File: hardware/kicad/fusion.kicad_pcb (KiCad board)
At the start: 2 copper layers, 33 x 59.9 mm, 36 parts, among them J1 BATTERY, J2 LSM6DSOX, J3 PICKIT, J4 HC-05, J5 FLEX, J7 FTDI, SW1 BUTTON, SW2 POWER, SW3 UART, U1 MCP1603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

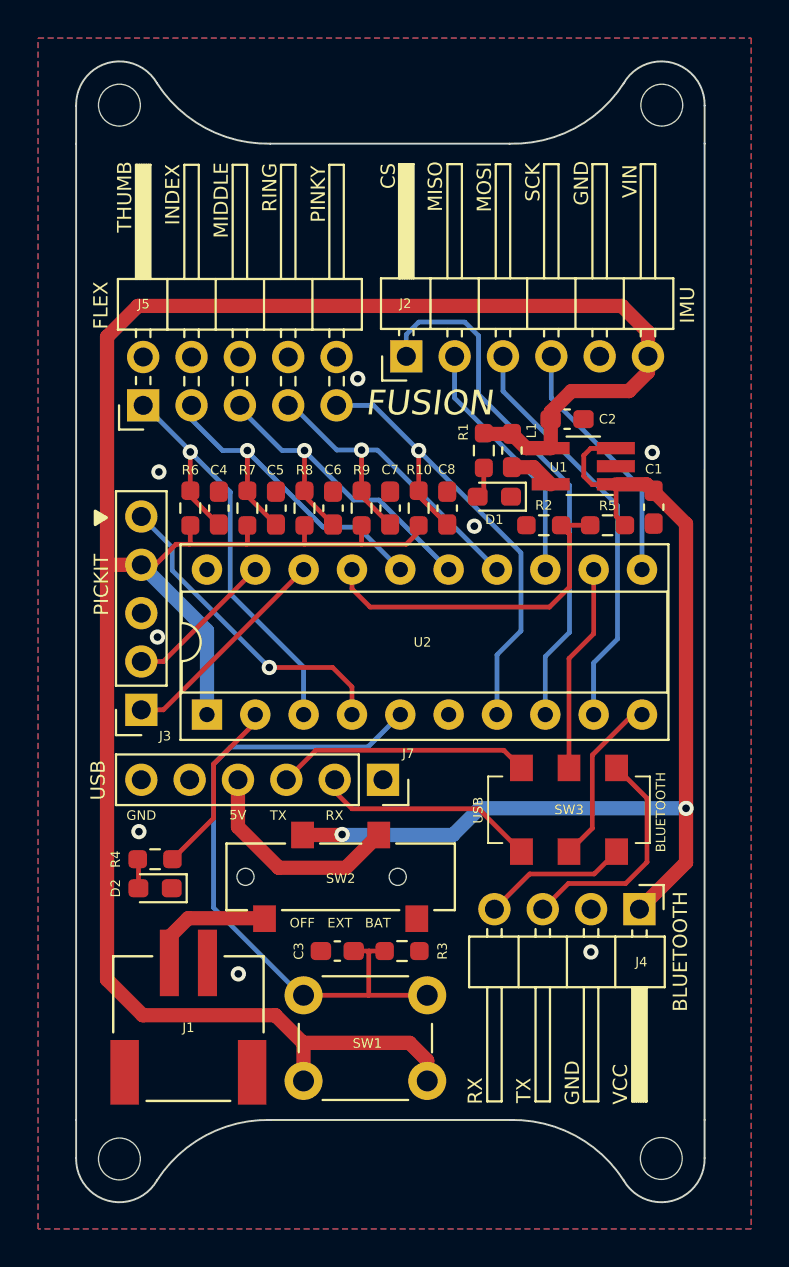
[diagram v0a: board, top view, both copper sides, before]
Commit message: Better ground stitching and silk fix for power switch
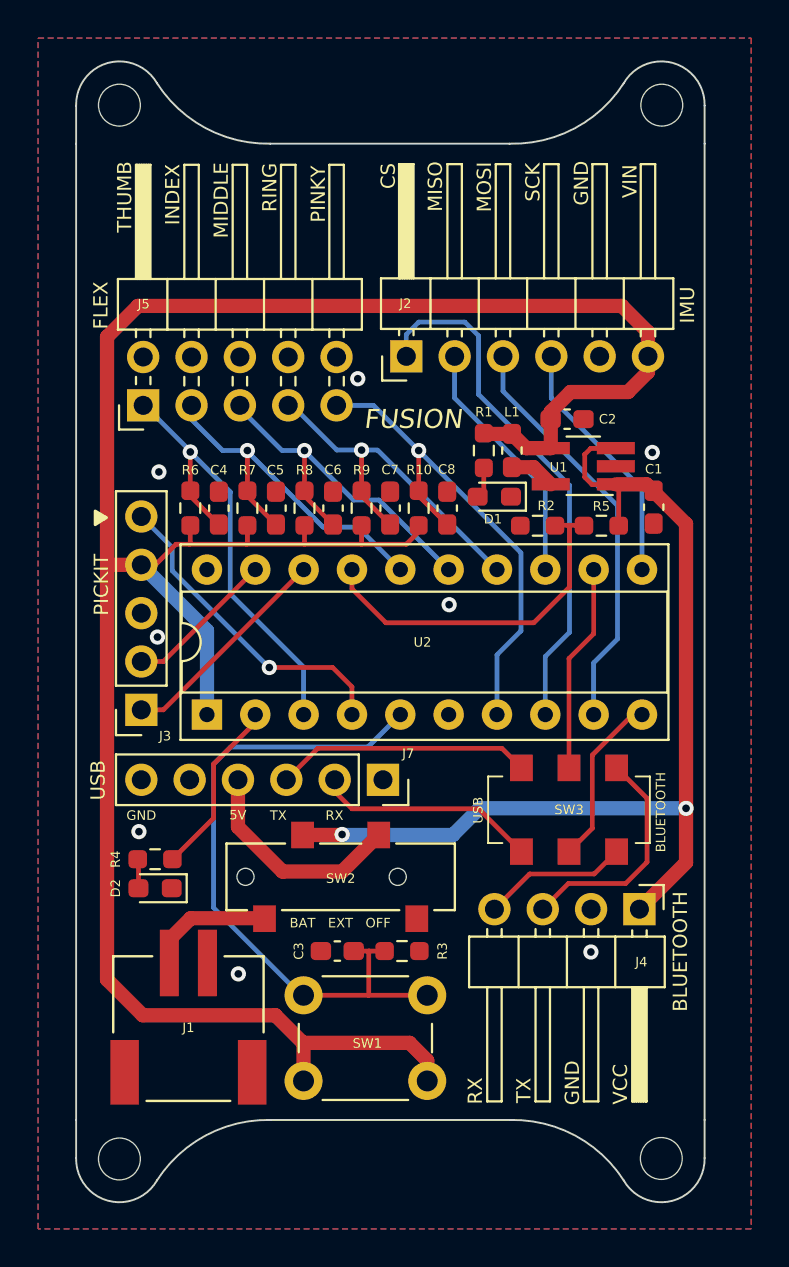
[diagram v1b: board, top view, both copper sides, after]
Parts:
- moved R5 0.33 mm to (164.6, 88.1)
- moved R2 0.33 mm to (161.2, 88.1)
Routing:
- net Net-(J1-Pad1): track 6.68 -> 5.38 mm
- net USB_RX: track 11.7 -> 11.1 mm
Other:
- board text added: "BAT EXT OFF"
- board text removed: "OFF EXT BAT"

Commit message: Change LED resistors to 200R (DigiKey availability)
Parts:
- R1, R4: value 270R -> 200R
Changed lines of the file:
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@@
       (effects (font (size 0.5 0.5) (thickness 0.1)))
     )
-    (fp_text value "270R" (at 0 1.43) (layer "F.Fab")
+    (fp_text value "200R" (at 0 1.43) (layer "F.Fab")
       (effects (font (size 1 1) (thickness 0.15)))
     )
@@
       (effects (font (size 0.5 0.5) (thickness 0.1)))
     )
-    (fp_text value "270R" (at 0 1.43 90) (layer "F.Fab")
-      (effects (font (size 1 1) (thickness 0.15)))
-    )
+    (fp_text value "200R" (at 0 1.43 90) (layer "F.Fab")
+      (effects (font (size 1 1) (thickness 0.15)))
+    )

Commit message: Implement Chung's feedback for PCB
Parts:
- moved R1 21.9 mm to (163.1, 105.5), turned to 0 degrees
- moved C2 21.0 mm to (167.1, 103.1), turned to 90 degrees
- moved L1 19.8 mm to (165.6, 103.0), turned to -90 degrees
- moved D1 19.0 mm to (159.7, 105.5), turned to 0 degrees
- moved C1 18.4 mm to (158.1, 103.0)
- moved U1 18.1 mm to (161.8, 103.0), turned to 0 degrees
- moved SW3 17.6 mm to (163.1, 85.4)
- moved R5 13.4 mm to (159.7, 100.5), turned to 0 degrees
- moved R2 12.6 mm to (163.1, 100.5), turned to 0 degrees
- moved REF** 1.00 mm to (139.3, 67.0)
- moved REF** 1.00 mm to (167.8, 67.0)
- moved J2 0.78 mm to (154.2, 80.0)
- moved J5 0.78 mm to (140.4, 82.5)
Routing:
- net BT_RX: track 7.67 -> 26.7 mm, vias 0 -> 1
- net BT_TX: track 12.1 -> 31.0 mm, vias 0 -> 1
- net VDC: track 53.3 -> 37.1 mm
- net USB_TX: track 13.5 -> 24.5 mm
- net USB_RX: track 11.1 -> 18.8 mm
- net RX: track 11.0 -> 7.55 mm
- net +3V3: track 129.3 -> 125.9 mm
- net TX: track 8.59 -> 11.8 mm
- net GNDREF: track 0.00 -> 2.35 mm, vias 8 -> 12
- net MCLR: track 17.0 -> 18.4 mm
- net CS: track 27.9 -> 26.7 mm
- net PINKY: track 26.2 -> 27.2 mm
- net SCK: track 13.2 -> 12.4 mm
- net MISO: track 13.2 -> 12.4 mm
- net MOSI: track 21.8 -> 21.1 mm
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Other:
- board size 33 x 59.9 mm -> 33 x 58.9 mm
- board text added: "v1.0"

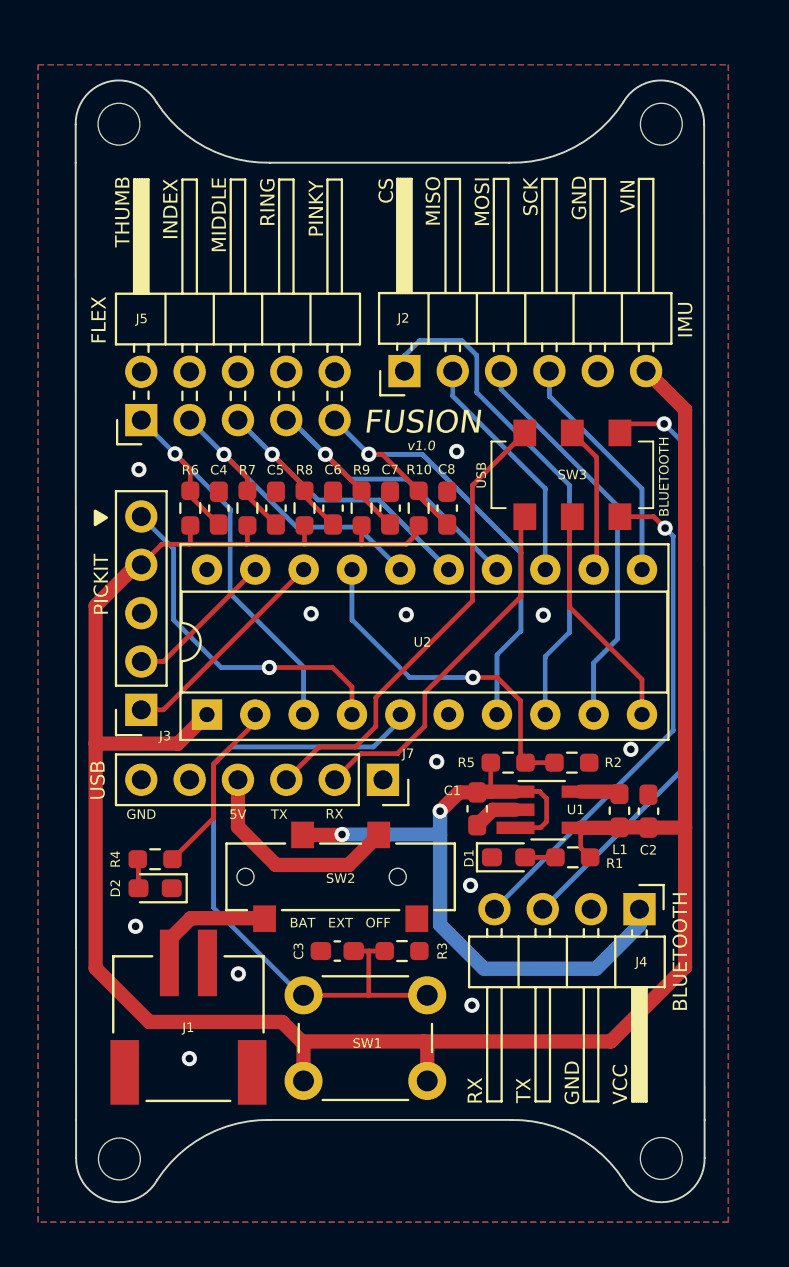
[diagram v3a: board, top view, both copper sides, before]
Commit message: small routing changes
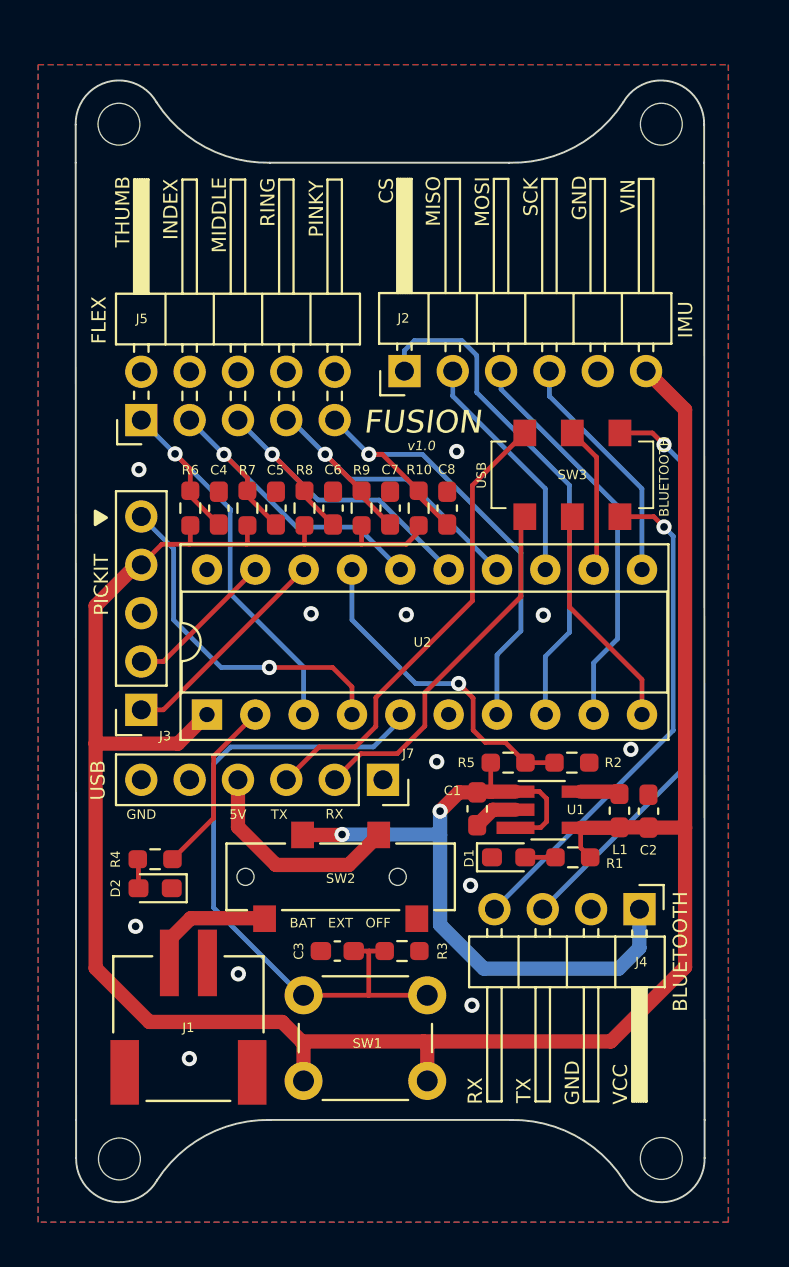
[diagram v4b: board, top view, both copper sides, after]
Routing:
- net VBAT_ADC: track 18.1 -> 17.4 mm
- net VDC: track 37.1 -> 37.7 mm
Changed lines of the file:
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@@
     (effects (font (size 0.5 0.5) (thickness 0.1)))
   )
+  (segment (start 154.25 78.8712) (end 154.25 79.95) (width 0.25) (layer "B.Cu") (net 1))
+  (segment (start 157.275 78.35) (end 154.7712 78.35) (width 0.25) (layer "B.Cu") (net 1))
+  (segment (start 154.7712 78.35) (end 154.25 78.8712) (width 0.25) (layer "B.Cu") (net 1))
+  (segment (start 161.655 98) (end 161.655 94.945) (width 0.25) (layer "B.Cu") (net 1))
+  (segment (start 158.05 79.125) (end 157.275 78.35) (width 0.25) (layer "B.Cu") (net 1))
+  (segment (start 162.925 85.95) (end 158.05 81.075) (width 0.25) (layer "B.Cu") (net 1))
   (segment (start 162.925 93.675) (end 162.925 85.95) (width 0.25) (layer "B.Cu") (net 1))
-  (segment (start 158.05 79.125) (end 157.275 78.35) (width 0.25) (layer "B.Cu") (net 1))
-  (segment (start 155.05 78.35) (end 154.25 79.15) (width 0.25) (layer "B.Cu") (net 1))
+  (segment (start 161.655 94.945) (end 162.925 93.675) (width 0.25) (layer "B.Cu") (net 1))
   (segment (start 158.05 81.075) (end 158.05 79.125) (width 0.25) (layer "B.Cu") (net 1))
-  (segment (start 154.25 79.15) (end 154.25 79.95) (width 0.25) (layer "B.Cu") (net 1))
-  (segment (start 157.275 78.35) (end 155.05 78.35) (width 0.25) (layer "B.Cu") (net 1))
-  (segment (start 161.655 94.945) (end 162.925 93.675) (width 0.25) (layer "B.Cu") (net 1))
-  (segment (start 162.925 85.95) (end 158.05 81.075) (width 0.25) (layer "B.Cu") (net 1))
-  (segment (start 161.655 98) (end 161.655 94.945) (width 0.25) (layer "B.Cu") (net 1))
   (segment (start 156.79 81.265) (end 161.655 86.13) (width 0.25) (layer "B.Cu") (net 2))
   (segment (start 161.655 86.13) (end 161.655 90.38) (width 0.25) (layer "B.Cu") (net 2))
@@
   (segment (start 142.125 89.29) (end 140.425 87.59) (width 0.25) (layer "B.Cu") (net 9))
   (segment (start 142.125 93.025) (end 142.125 89.29) (width 0.25) (layer "B.Cu") (net 9))
-  (segment (start 167.9 82.725) (end 166.05 82.725) (width 0.25) (layer "F.Cu") (net 10))
-  (via (at 167.9 82.725) (size 0.8) (drill 0.4) (layers "F.Cu" "B.Cu") (net 10))
-  (segment (start 167.9 82.725) (end 169.075 83.9) (width 0.25) (layer "B.Cu") (net 10))
-  (segment (start 169.075 83.9) (end 169.075 100.67) (width 0.25) (layer "B.Cu") (net 10))
+  (segment (start 167.28 83.2) (end 167.9 83.82) (width 0.25) (layer "F.Cu") (net 10))
+  (segment (start 165.575 83.2) (end 167.28 83.2) (width 0.25) (layer "F.Cu") (net 10))
+  (via (at 167.894 83.82) (size 0.8) (drill 0.4) (layers "F.Cu" "B.Cu") (net 10))
   (segment (start 169.075 100.67) (end 161.52 108.225) (width 0.25) (layer "B.Cu") (net 10))
-  (segment (start 167.95 88.2) (end 167.35 87.6) (width 0.25) (layer "F.Cu") (net 11))
-  (segment (start 167.35 87.6) (end 165.575 87.6) (width 0.25) (layer "F.Cu") (net 11))
-  (via (at 167.95 88.2) (size 0.8) (drill 0.4) (layers "F.Cu" "B.Cu") (net 11))
+  (segment (start 169.075 84.995) (end 169.075 100.67) (width 0.25) (layer "B.Cu") (net 10))
+  (segment (start 167.9 83.82) (end 169.075 84.995) (width 0.25) (layer "B.Cu") (net 10))
+  (segment (start 165.575 87.6) (end 167.356 87.6) (width 0.25) (layer "F.Cu") (net 11))
+  (segment (start 167.356 87.6) (end 167.894 88.138) (width 0.25) (layer "F.Cu") (net 11))
+  (via (at 167.894 88.138) (size 0.8) (drill 0.4) (layers "F.Cu" "B.Cu") (net 11))
+  (segment (start 168.375 88.619) (end 168.375 98.83) (width 0.25) (layer "B.Cu") (net 11))
+  (segment (start 167.894 88.138) (end 168.375 88.619) (width 0.25) (layer "B.Cu") (net 11))
   (segment (start 168.375 98.83) (end 158.98 108.225) (width 0.25) (layer "B.Cu") (net 11))
-  (segment (start 167.95 88.2) (end 168.375 88.625) (width 0.25) (layer "B.Cu") (net 11))
-  (segment (start 168.375 88.625) (end 168.375 98.83) (width 0.25) (layer "B.Cu") (net 11))
   (segment (start 155 86.2375) (end 153.0825 84.32) (width 0.25) (layer "F.Cu") (net 12))
   (segment (start 155 86.5125) (end 156.5 88.0125) (width 0.25) (layer "F.Cu") (net 12))
@@
   (segment (start 160.375 89.5) (end 160.375 93.6) (width 0.25) (layer "B.Cu") (net 12))
   (segment (start 152.385 84.325) (end 155.2 84.325) (width 0.25) (layer "B.Cu") (net 12))
+  (segment (start 150.0886 84.3261) (end 152 86.2375) (width 0.25) (layer "F.Cu") (net 13))
   (segment (start 152 86.5125) (end 153.5 88.0125) (width 0.25) (layer "F.Cu") (net 13))
-  (segment (start 150.1 84.325) (end 152 86.225) (width 0.25) (layer "F.Cu") (net 13))
-  (via (at 150.1 84.325) (size 0.8) (drill 0.4) (layers "F.Cu" "B.Cu") (net 13))
-  (segment (start 151.4 85.625) (end 154.36 85.625) (width 0.25) (layer "B.Cu") (net 13))
-  (segment (start 150.1 84.325) (end 151.4 85.625) (width 0.25) (layer "B.Cu") (net 13))
+  (segment (start 150.0886 84.325) (end 150.0886 84.3261) (width 0.25) (layer "F.Cu") (net 13))
+  (via (at 150.0886 84.3225) (size 0.8) (drill 0.4) (layers "F.Cu" "B.Cu") (net 13))
+  (segment (start 150.0886 84.3225) (end 148.2911 82.525) (width 0.25) (layer "B.Cu") (net 13))
   (segment (start 154.36 85.625) (end 159.115 90.38) (width 0.25) (layer "B.Cu") (net 13))
-  (segment (start 148.3 82.525) (end 150.1 84.325) (width 0.25) (layer "B.Cu") (net 13))
+  (segment (start 151.3886 85.625) (end 154.36 85.625) (width 0.25) (layer "B.Cu") (net 13))
+  (segment (start 150.0886 84.325) (end 151.3886 85.625) (width 0.25) (layer "B.Cu") (net 13))
   (segment (start 149 86.02) (end 147.3025 84.3225) (width 0.25) (layer "F.Cu") (net 14))
   (segment (start 149 86.5125) (end 150.5 88.0125) (width 0.25) (layer "F.Cu") (net 14))
@@
   (via (at 150.975 104.3) (size 0.8) (drill 0.4) (layers "F.Cu" "B.Cu") (net 26))
   (via (at 156.125 103.075) (size 0.8) (drill 0.4) (layers "F.Cu" "B.Cu") (net 26))
-  (segment (start 164.325 111.35) (end 166.6 109.075) (width 0.75) (layer "B.Cu") (net 26))
-  (segment (start 158.425 111.35) (end 164.325 111.35) (width 0.75) (layer "B.Cu") (net 26))
   (segment (start 156.125 103.075) (end 156.125 104.325) (width 0.75) (layer "B.Cu") (net 26))
   (segment (start 156.1 104.3) (end 156.125 104.325) (width 0.75) (layer "B.Cu") (net 26))
   (segment (start 156.125 104.325) (end 156.125 109.05) (width 0.75) (layer "B.Cu") (net 26))
   (segment (start 150.975 104.3) (end 156.1 104.3) (width 0.75) (layer "B.Cu") (net 26))
-  (segment (start 166.6 109.075) (end 166.6 108.225) (width 0.75) (layer "B.Cu") (net 26))
+  (segment (start 158.425 111.35) (end 165.51 111.35) (width 0.75) (layer "B.Cu") (net 26))
+  (segment (start 166.6 110.26) (end 166.6 108.225) (width 0.75) (layer "B.Cu") (net 26))
+  (segment (start 165.51 111.35) (end 166.6 110.26) (width 0.75) (layer "B.Cu") (net 26))
   (segment (start 156.125 109.05) (end 158.425 111.35) (width 0.75) (layer "B.Cu") (net 26))
   (segment (start 165.425 102.05) (end 165.55 102.175) (width 0.75) (layer "F.Cu") (net 27))
   (segment (start 163.51 102.05) (end 165.425 102.05) (width 0.75) (layer "F.Cu") (net 27))
-  (segment (start 146.415 98.41) (end 144.225 100.6) (width 0.25) (layer "F.Cu") (net 28))
-  (segment (start 144.225 100.6) (end 144.225 103.4375) (width 0.25) (layer "F.Cu") (net 28))
+  (segment (start 146.415 98) (end 144.225 100.19) (width 0.25) (layer "F.Cu") (net 28))
+  (segment (start 144.225 100.19) (end 144.225 103.4375) (width 0.25) (layer "F.Cu") (net 28))
   (segment (start 144.225 103.4375) (end 142.1 105.5625) (width 0.25) (layer "F.Cu") (net 28))
-  (segment (start 160.35 100.2625) (end 160.6125 100.525) (width 0.25) (layer "F.Cu") (net 29))
-  (segment (start 159.125 96.05) (end 160.35 97.275) (width 0.25) (layer "F.Cu") (net 29))
+  (segment (start 159.5539 99.4664) (end 160.6125 100.525) (width 0.25) (layer "F.Cu") (net 29))
+  (segment (start 157.861 98.816184) (end 158.511216 99.4664) (width 0.25) (layer "F.Cu") (net 29))
+  (segment (start 157.099 96.3676) (end 157.861 97.1296) (width 0.25) (layer "F.Cu") (net 29))
   (segment (start 160.6125 100.525) (end 162.1375 100.525) (width 0.25) (layer "F.Cu") (net 29))
-  (segment (start 160.35 97.275) (end 160.35 100.2625) (width 0.25) (layer "F.Cu") (net 29))
-  (segment (start 157.85 96.05) (end 159.125 96.05) (width 0.25) (layer "F.Cu") (net 29))
-  (via (at 157.85 96.05) (size 0.8) (drill 0.4) (layers "F.Cu" "B.Cu") (net 29))
-  (segment (start 154.525 96.05) (end 151.495 93.02) (width 0.25) (layer "B.Cu") (net 29))
+  (segment (start 157.861 97.1296) (end 157.861 98.816184) (width 0.25) (layer "F.Cu") (net 29))
+  (segment (start 158.511216 99.4664) (end 159.5539 99.4664) (width 0.25) (layer "F.Cu") (net 29))
+  (via (at 157.099 96.3676) (size 0.8) (drill 0.4) (layers "F.Cu" "B.Cu") (net 29))
   (segment (start 151.495 93.02) (end 151.495 90.38) (width 0.25) (layer "B.Cu") (net 29))
-  (segment (start 157.85 96.05) (end 154.525 96.05) (width 0.25) (layer "B.Cu") (net 29))
+  (segment (start 157.099 96.3676) (end 154.8426 96.3676) (width 0.25) (layer "B.Cu") (net 29))
+  (segment (start 154.8426 96.3676) (end 151.495 93.02) (width 0.25) (layer "B.Cu") (net 29))
   (segment (start 140.275 107.125) (end 140.275 105.6375) (width 0.25) (layer "F.Cu") (net 30))
   (segment (start 141.9 109.825) (end 143.025 108.7) (width 0.75) (layer "F.Cu") (net 32))
